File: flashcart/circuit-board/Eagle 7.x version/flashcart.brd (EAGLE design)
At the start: 30.5 x 12.7 mm, 17 parts, among them U1 MCP1700T-3302E/TT, U2 TXB0104D, U3 W25Q128FV

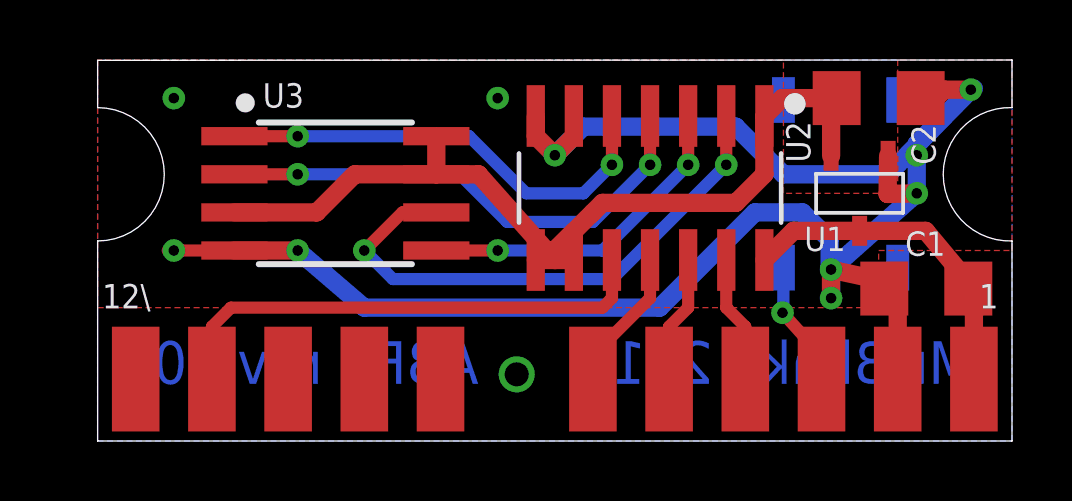
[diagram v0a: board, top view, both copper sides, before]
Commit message: rev1.1 + gerbers
Changed connector pads, minor tweaks, added Blinky icon, added gerbers
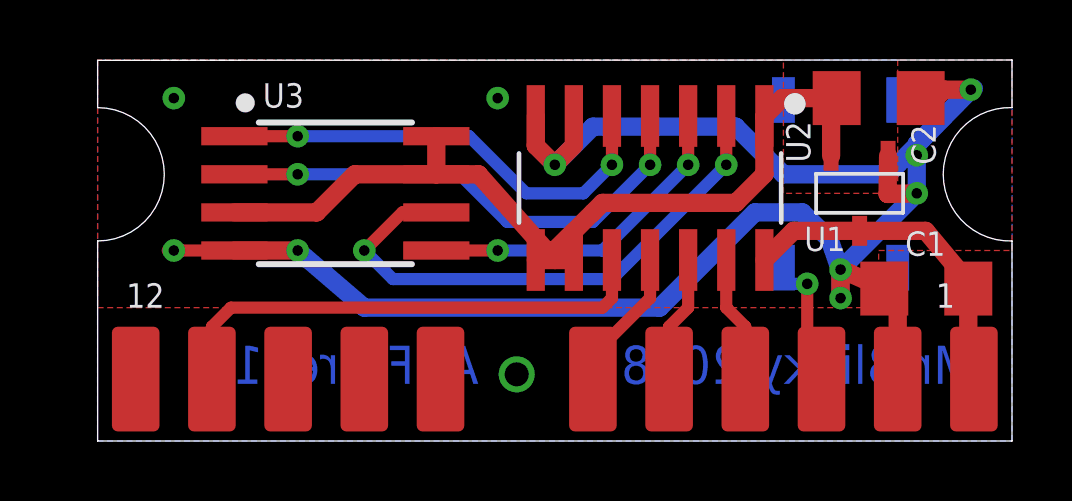
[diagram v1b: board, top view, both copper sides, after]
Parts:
- removed 1, 10, 11, 12\, 2, 3, 4, 5, 6, 8, 9: (no value), wirepad:SMD1,27-2,54
- added CON1: AB-CON, ab-expansion-con:CON-PAC
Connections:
- net GND: now also CON1.2; no longer 2.1
- net MISO: now also CON1.6; no longer 6.1
- net MOSI: now also CON1.5; no longer 5.1
- net NC: now also CON1.8; no longer 8.1
- net RESET: now also CON1.3; no longer 3.1
- net RX: now also CON1.11; no longer 11.1
- net SCK: now also CON1.4; no longer 4.1
- net SCL: now also CON1.10; no longer 10.1
- net SDA: now also CON1.9; no longer 9.1
- net TX: now also CON1.12; no longer 12\.1
- net VCC: now also CON1.1; no longer 1.1
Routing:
- net RESET: track 4.42 -> 5.46 mm
- net GND: track 62.6 -> 63.1 mm
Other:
- board text added: "ABFC rev1.1"
- board text added: "C:/Users/Blinky/Desktop/mrblinky-monochrome.bmp"
- board text removed: "ABFC rev1.0"
